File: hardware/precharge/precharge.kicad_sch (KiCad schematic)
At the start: 12 parts

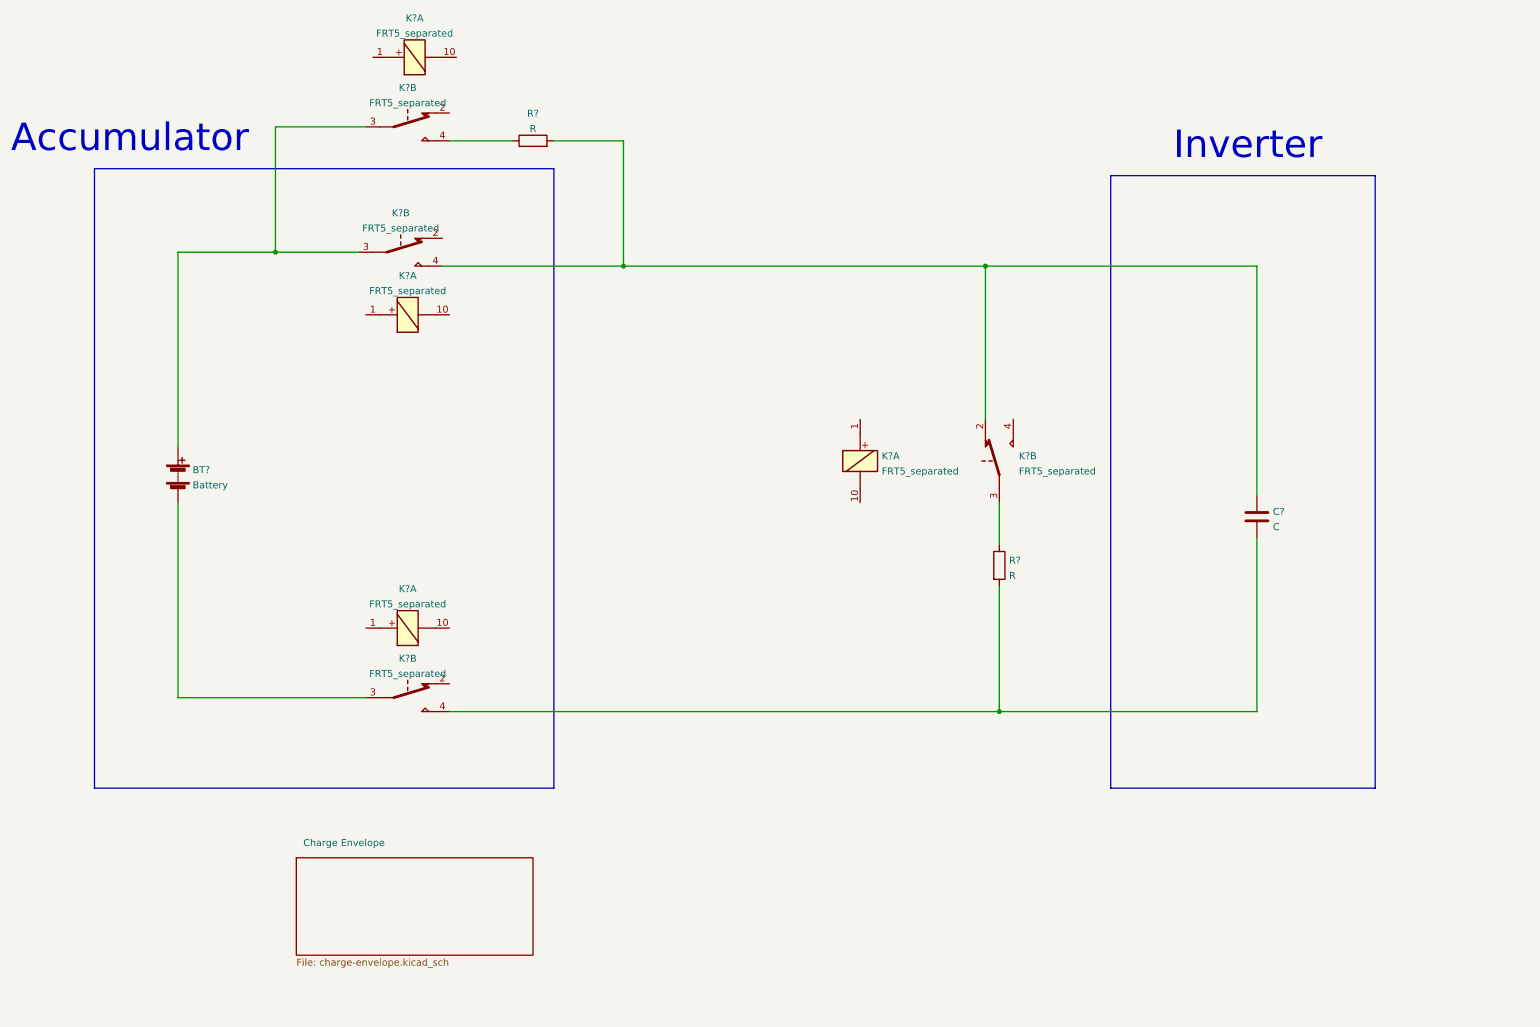
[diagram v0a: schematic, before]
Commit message: The precharge needs to be inside the accumulator housing
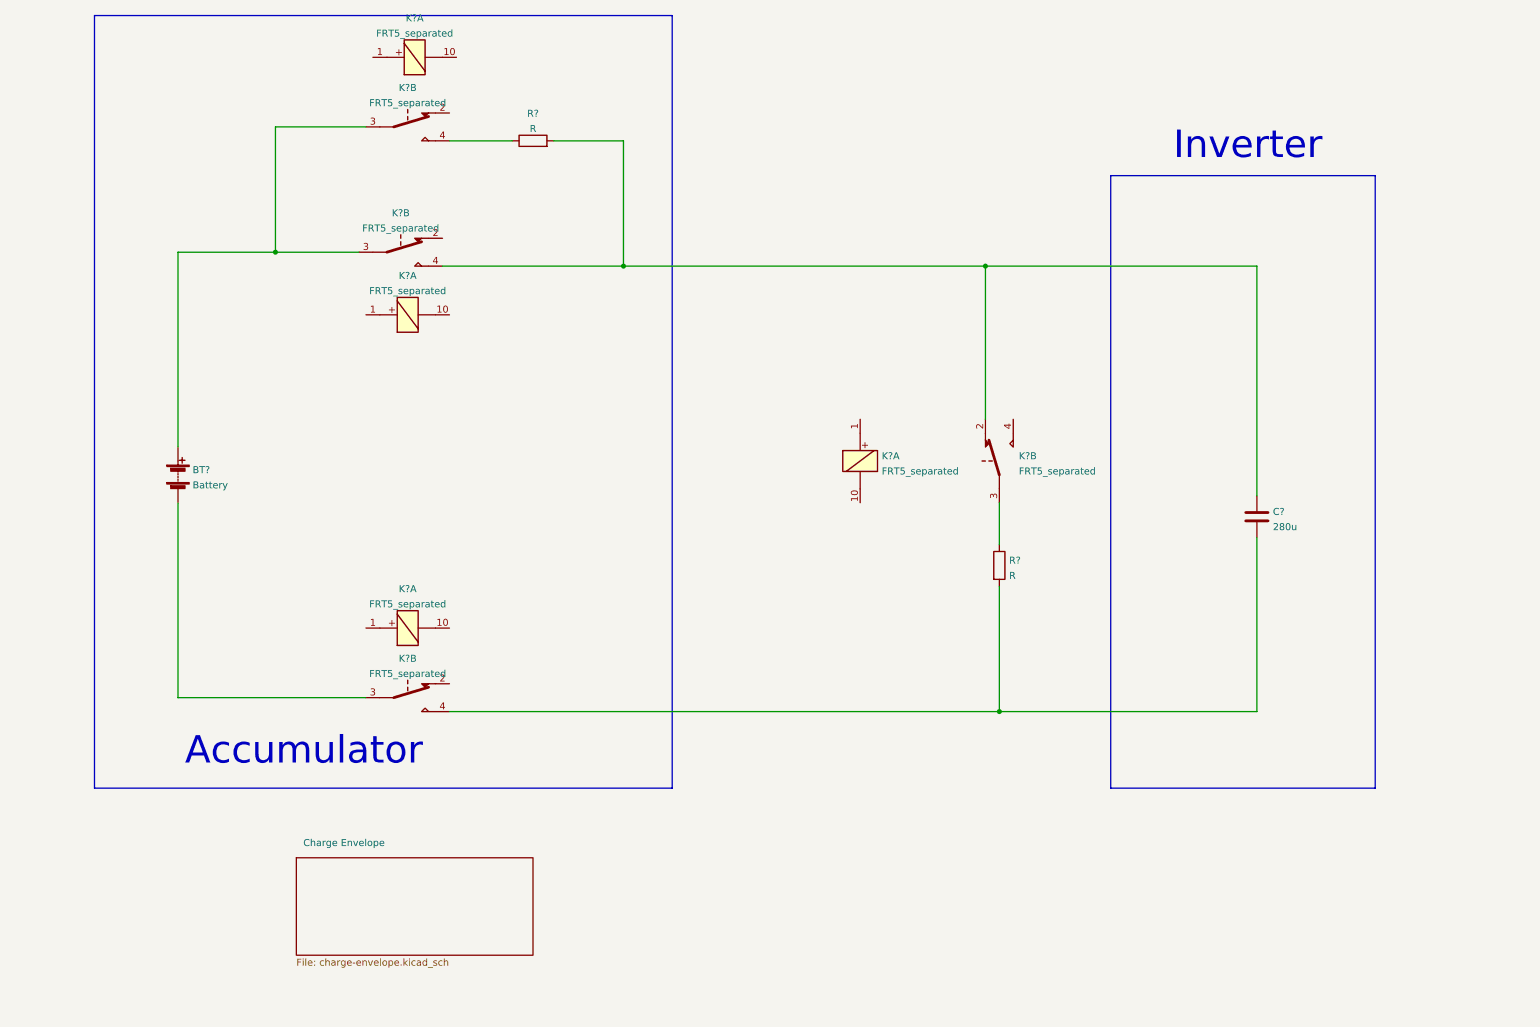
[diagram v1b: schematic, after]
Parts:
- C?: value C -> 280u
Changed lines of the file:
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@@
     (stroke (width 1) (type default) (color 0 0 0 0))
   )
-  (polyline (pts (xy 29.21 41.91) (xy 29.21 154.94))
-    (stroke (width 0) (type default) (color 0 0 0 0))
-  )
-  (polyline (pts (xy 29.21 41.91) (xy 113.03 41.91))
-    (stroke (width 0) (type default) (color 0 0 0 0))
-  )
-  (polyline (pts (xy 113.03 41.91) (xy 113.03 154.94))
-    (stroke (width 0) (type default) (color 0 0 0 0))
-  )
-  (polyline (pts (xy 113.03 154.94) (xy 29.21 154.94))
+  (polyline (pts (xy 29.21 13.97) (xy 29.21 154.94))
+    (stroke (width 0) (type default) (color 0 0 0 0))
+  )
+  (polyline (pts (xy 29.21 13.97) (xy 134.62 13.97))
+    (stroke (width 0) (type default) (color 0 0 0 0))
+  )
+  (polyline (pts (xy 134.62 13.97) (xy 134.62 154.94))
+    (stroke (width 0) (type default) (color 0 0 0 0))
+  )
+  (polyline (pts (xy 134.62 154.94) (xy 29.21 154.94))
     (stroke (width 0) (type default) (color 0 0 0 0))
   )
@@
     (stroke (width 0) (type default) (color 0 0 0 0))
   )
-  (text "Accumulator" (at 13.97 39.37 0)
+  (text "Accumulator" (at 45.72 151.13 0)
     (effects (font (size 5 5)) (justify left bottom))
   )
@@
       (effects (font (size 1.27 1.27)) (justify left))
     )
-    (property "Value" "C" (id 1) (at 244.221 107.2766 0)
+    (property "Value" "280u" (id 1) (at 244.221 107.2766 0)
       (effects (font (size 1.27 1.27)) (justify left))
     )
@@
     )
     (path "/5331a353-bd34-472d-a07a-36301f80c77e"
-      (reference "C?") (unit 1) (value "C") (footprint "")
+      (reference "C?") (unit 1) (value "280u") (footprint "")
     )
     (path "/00f0519b-5f92-462f-871a-9c64c0c176a6"

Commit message: Add circuitry to make use of the inverter's analogue inputs and relay outputs
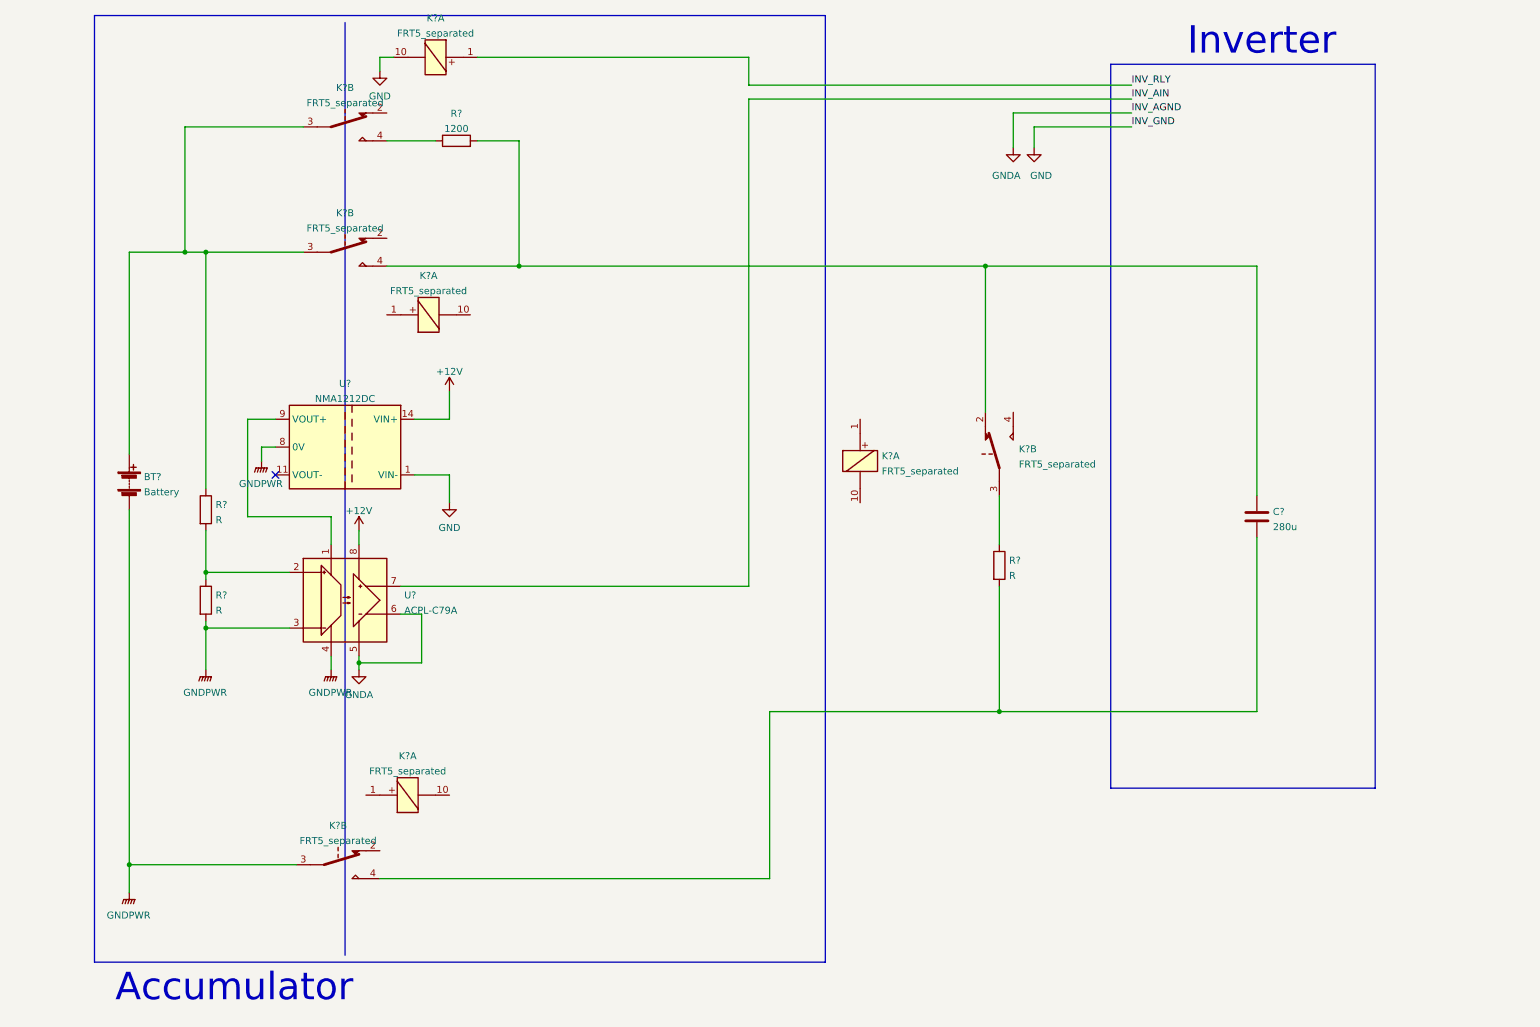
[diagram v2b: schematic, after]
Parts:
- added R? (x2): R, symbol Device:R
- added U?: NMA1212DC, Converter_DCDC:Converter_DCDC_muRata_NMAxxxxDC_THT, symbol Regulator_Switching:NMA1212DC
- added U?: ACPL-C79A, Package_SO:SSO-8_6.8x5.9mm_P1.27mm_Clearance8mm, symbol Isolator_Analog:ACPL-C79A
- R?: value R -> 1200
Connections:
- net at BT?.1 (+), K?.3, K?.3: now also R?.1
- net INV_RLY: now reaches K?.1
- net GND: now reaches K?.10
- net GND: now also U?.1 (VIN-)
- net GNDPWR: now reaches BT?.2 (-), K?.3
- net GNDPWR: now also R?.2, U?.3 (IN-), U?.4 (GND1), U?.8 (0V)
- new net: U?.1 (VDD1), U?.9 (VOUT+)
- new net: R?.1, R?.2, U?.2 (IN+)
- new net +12V: U?.14 (VIN+), U?.8 (VDD2)
- new net GNDA: U?.5 (GND2), U?.6 (OUT-)
- new net INV_AIN: U?.7 (OUT+)
- no-connect marks 0 -> 1
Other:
- removed sheet Charge Envelope
- moved on the sheet: BT?, K?A, K?B, R?

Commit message: ???
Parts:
- R?: value R -> 3000
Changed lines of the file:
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@@
 (kicad_sch (version 20210621) (generator eeschema)
   (paper "A4")
+  (junction (at 194.31 140.97) (diameter 0) (color 0 0 0 0))
+  (junction (at 35.56 168.91) (diameter 0) (color 0 0 0 0))
+  (junction (at 106.68 59.69) (diameter 0) (color 0 0 0 0))
   (junction (at 191.77 59.69) (diameter 0) (color 0 0 0 0))
-  (junction (at 194.31 140.97) (diameter 0) (color 0 0 0 0))
-  (junction (at 106.68 59.69) (diameter 0) (color 0 0 0 0))
+  (junction (at 77.47 132.08) (diameter 0) (color 0 0 0 0))
   (junction (at 49.53 115.57) (diameter 0) (color 0 0 0 0))
-  (junction (at 77.47 132.08) (diameter 0) (color 0 0 0 0))
-  (junction (at 35.56 168.91) (diameter 0) (color 0 0 0 0))
+  (junction (at 49.53 125.73) (diameter 0) (color 0 0 0 0))
   (junction (at 45.72 57.15) (diameter 0) (color 0 0 0 0))
-  (junction (at 49.53 125.73) (diameter 0) (color 0 0 0 0))
   (junction (at 49.53 57.15) (diameter 0) (color 0 0 0 0))
   (no_connect (at 62.23 97.79))
+  (wire (pts (xy 152.4 171.45) (xy 152.4 140.97))
+    (stroke (width 1) (type default) (color 0 0 0 0))
+  )
+  (wire (pts (xy 81.28 171.45) (xy 152.4 171.45))
+    (stroke (width 1) (type default) (color 0 0 0 0))
+  )
   (wire (pts (xy 152.4 140.97) (xy 194.31 140.97))
     (stroke (width 1) (type default) (color 0 0 0 0))
   )
-  (wire (pts (xy 152.4 171.45) (xy 152.4 140.97))
-    (stroke (width 1) (type default) (color 0 0 0 0))
-  )
-  (wire (pts (xy 81.28 171.45) (xy 152.4 171.45))
-    (stroke (width 1) (type default) (color 0 0 0 0))
-  )
   (wire (pts (xy 35.56 168.91) (xy 35.56 173.99))
     (stroke (width 1) (type default) (color 0 0 0 0))
@@
     (stroke (width 0) (type default) (color 0 0 0 0))
   )
+  (wire (pts (xy 57.15 105.41) (xy 72.39 105.41))
+    (stroke (width 0) (type default) (color 0 0 0 0))
+  )
+  (wire (pts (xy 72.39 105.41) (xy 72.39 110.49))
+    (stroke (width 0) (type default) (color 0 0 0 0))
+  )
   (wire (pts (xy 62.23 87.63) (xy 57.15 87.63))
     (stroke (width 0) (type default) (color 0 0 0 0))
   )
-  (wire (pts (xy 57.15 105.41) (xy 72.39 105.41))
-    (stroke (width 0) (type default) (color 0 0 0 0))
-  )
   (wire (pts (xy 57.15 87.63) (xy 57.15 105.41))
     (stroke (width 0) (type default) (color 0 0 0 0))
   )
-  (wire (pts (xy 72.39 105.41) (xy 72.39 110.49))
-    (stroke (width 0) (type default) (color 0 0 0 0))
-  )
   (wire (pts (xy 93.98 82.55) (xy 93.98 87.63))
     (stroke (width 0) (type default) (color 0 0 0 0))
@@
     (stroke (width 1) (type default) (color 0 0 0 0))
   )
+  (wire (pts (xy 81.28 21.59) (xy 81.28 24.13))
+    (stroke (width 0) (type default) (color 0 0 0 0))
+  )
   (wire (pts (xy 83.82 21.59) (xy 81.28 21.59))
     (stroke (width 0) (type default) (color 0 0 0 0))
   )
-  (wire (pts (xy 81.28 21.59) (xy 81.28 24.13))
-    (stroke (width 0) (type default) (color 0 0 0 0))
-  )
   (wire (pts (xy 72.39 130.81) (xy 72.39 133.35))
     (stroke (width 0) (type default) (color 0 0 0 0))
   )
+  (wire (pts (xy 241.3 101.6) (xy 241.3 59.69))
+    (stroke (width 1) (type default) (color 0 0 0 0))
+  )
+  (wire (pts (xy 191.77 59.69) (xy 106.68 59.69))
+    (stroke (width 1) (type default) (color 0 0 0 0))
+  )
   (wire (pts (xy 241.3 59.69) (xy 191.77 59.69))
     (stroke (width 1) (type default) (color 0 0 0 0))
   )
-  (wire (pts (xy 241.3 101.6) (xy 241.3 59.69))
-    (stroke (width 1) (type default) (color 0 0 0 0))
-  )
-  (wire (pts (xy 191.77 59.69) (xy 106.68 59.69))
-    (stroke (width 1) (type default) (color 0 0 0 0))
-  )
   (wire (pts (xy 194.31 101.6) (xy 194.31 110.49))
     (stroke (width 0) (type default) (color 0 0 0 0))
@@
     (stroke (width 0) (type default) (color 0 0 0 0))
   )
+  (polyline (pts (xy 214.63 22.86) (xy 214.63 154.94))
+    (stroke (width 0) (type default) (color 0 0 0 0))
+  )
+  (polyline (pts (xy 262.89 154.94) (xy 262.89 22.86))
+    (stroke (width 0) (type default) (color 0 0 0 0))
+  )
+  (polyline (pts (xy 214.63 22.86) (xy 262.89 22.86))
+    (stroke (width 0) (type default) (color 0 0 0 0))
+  )
   (polyline (pts (xy 214.63 154.94) (xy 262.89 154.94))
     (stroke (width 0) (type default) (color 0 0 0 0))
   )
-  (polyline (pts (xy 214.63 22.86) (xy 214.63 154.94))
-    (stroke (width 0) (type default) (color 0 0 0 0))
-  )
-  (polyline (pts (xy 262.89 154.94) (xy 262.89 22.86))
-    (stroke (width 0) (type default) (color 0 0 0 0))
-  )
-  (polyline (pts (xy 214.63 22.86) (xy 262.89 22.86))
-    (stroke (width 0) (type default) (color 0 0 0 0))
-  )
   (wire (pts (xy 77.47 107.95) (xy 77.47 110.49))
     (stroke (width 0) (type default) (color 0 0 0 0))
@@
     (stroke (width 0) (type default) (color 0 0 0 0))
   )
+  (wire (pts (xy 148.59 118.11) (xy 148.59 29.21))
+    (stroke (width 0) (type default) (color 0 0 0 0))
+  )
+  (wire (pts (xy 85.09 118.11) (xy 148.59 118.11))
+    (stroke (width 0) (type default) (color 0 0 0 0))
+  )
   (wire (pts (xy 148.59 29.21) (xy 218.44 29.21))
     (stroke (width 0) (type default) (color 0 0 0 0))
   )
-  (wire (pts (xy 148.59 118.11) (xy 148.59 29.21))
-    (stroke (width 0) (type default) (color 0 0 0 0))
-  )
-  (wire (pts (xy 85.09 118.11) (xy 148.59 118.11))
+  (polyline (pts (xy 29.21 13.97) (xy 29.21 186.69))
+    (stroke (width 0) (type default) (color 0 0 0 0))
+  )
+  (polyline (pts (xy 162.56 13.97) (xy 162.56 186.69))
+    (stroke (width 0) (type default) (color 0 0 0 0))
+  )
+  (polyline (pts (xy 162.56 186.69) (xy 29.21 186.69))
     (stroke (width 0) (type default) (color 0 0 0 0))
   )
@@
     (stroke (width 0) (type default) (color 0 0 0 0))
   )
-  (polyline (pts (xy 162.56 186.69) (xy 29.21 186.69))
-    (stroke (width 0) (type default) (color 0 0 0 0))
-  )
-  (polyline (pts (xy 29.21 13.97) (xy 29.21 186.69))
-    (stroke (width 0) (type default) (color 0 0 0 0))
-  )
-  (polyline (pts (xy 162.56 13.97) (xy 162.56 186.69))
-    (stroke (width 0) (type default) (color 0 0 0 0))
-  )
   (wire (pts (xy 49.53 57.15) (xy 49.53 100.33))
     (stroke (width 0) (type default) (color 0 0 0 0))
@@
     (stroke (width 0) (type default) (color 0 0 0 0))
   )
+  (wire (pts (xy 62.23 92.71) (xy 59.69 92.71))
+    (stroke (width 0) (type default) (color 0 0 0 0))
+  )
   (wire (pts (xy 59.69 92.71) (xy 59.69 95.25))
     (stroke (width 0) (type default) (color 0 0 0 0))
   )
-  (wire (pts (xy 62.23 92.71) (xy 59.69 92.71))
-    (stroke (width 0) (type default) (color 0 0 0 0))
-  )
   (wire (pts (xy 196.85 31.75) (xy 218.44 31.75))
     (stroke (width 0) (type default) (color 0 0 0 0))
@@
     (stroke (width 0) (type default) (color 0 0 0 0))
   )
+  (wire (pts (xy 35.56 104.14) (xy 35.56 168.91))
+    (stroke (width 1) (type default) (color 0 0 0 0))
+  )
   (wire (pts (xy 35.56 168.91) (xy 66.04 168.91))
-    (stroke (width 1) (type default) (color 0 0 0 0))
-  )
-  (wire (pts (xy 35.56 104.14) (xy 35.56 168.91))
     (stroke (width 1) (type default) (color 0 0 0 0))
   )
@@
       (effects (font (size 1.27 1.27)) (justify left))
     )
-    (property "Value" "R" (id 1) (at 196.088 116.1666 0)
+    (property "Value" "3000" (id 1) (at 196.088 116.1666 0)
       (effects (font (size 1.27 1.27)) (justify left))
     )
@@
     )
     (path "/b4de5946-04c7-4df0-883b-43022546f9fc"
-      (reference "R?") (unit 1) (value "R") (footprint "")
+      (reference "R?") (unit 1) (value "3000") (footprint "")
     )
     (path "/bf6c7fa0-d50c-4d12-9a1d-5261abd2ef28"
